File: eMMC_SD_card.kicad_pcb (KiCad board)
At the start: 4 copper layers, 100 x 74 mm, 362 parts, among them J1 SD_Card, J2 SD_Card, J3 SD_Card, J4 SD_Card, J5 SD_Card, J6 SD_Card, U1 eMMC_5.1_BGA153, U2 eMMC_5.1_BGA153, U3 eMMC_5.1_BGA153, U4 eMMC_5.1_BGA153, U5 eMMC_5.1_BGA153, U6 eMMC_5.1_BGA153

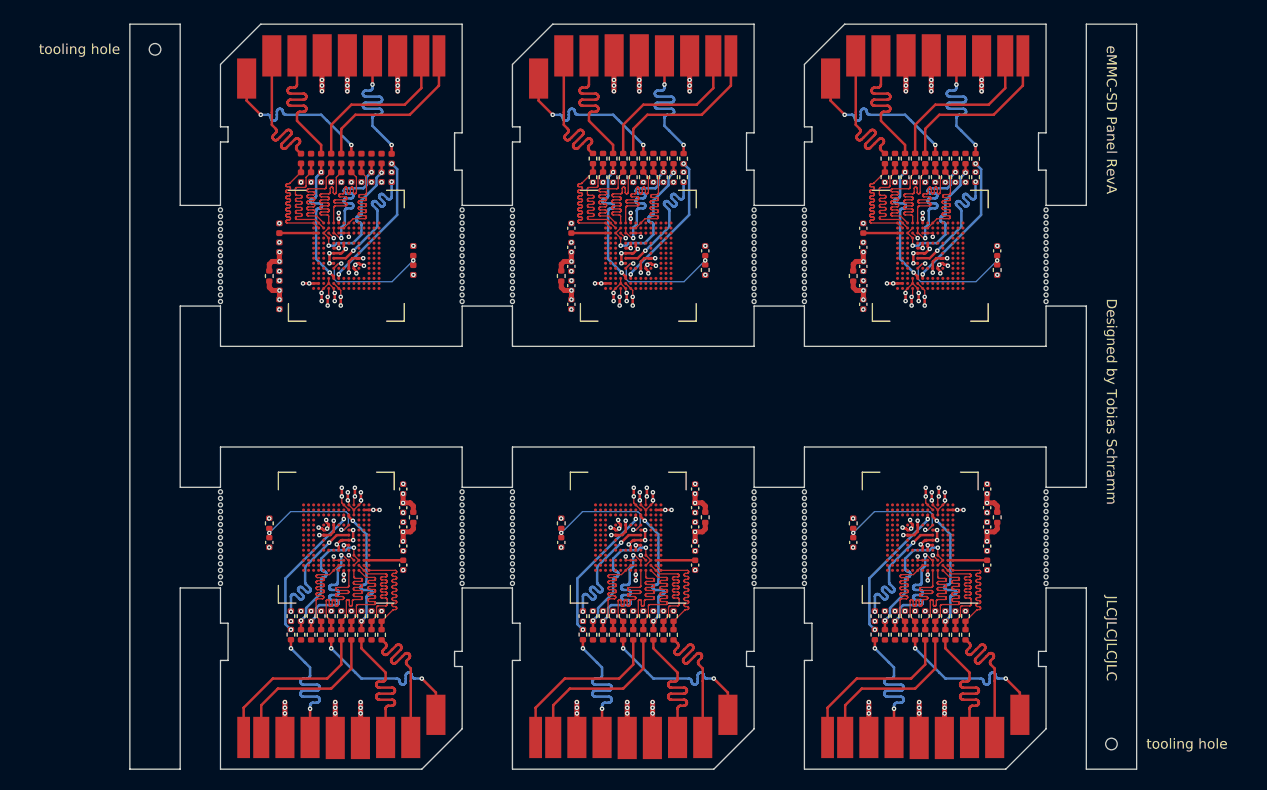
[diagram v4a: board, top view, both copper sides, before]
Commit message: Repurpose for ESP32 WiFi SDIO card
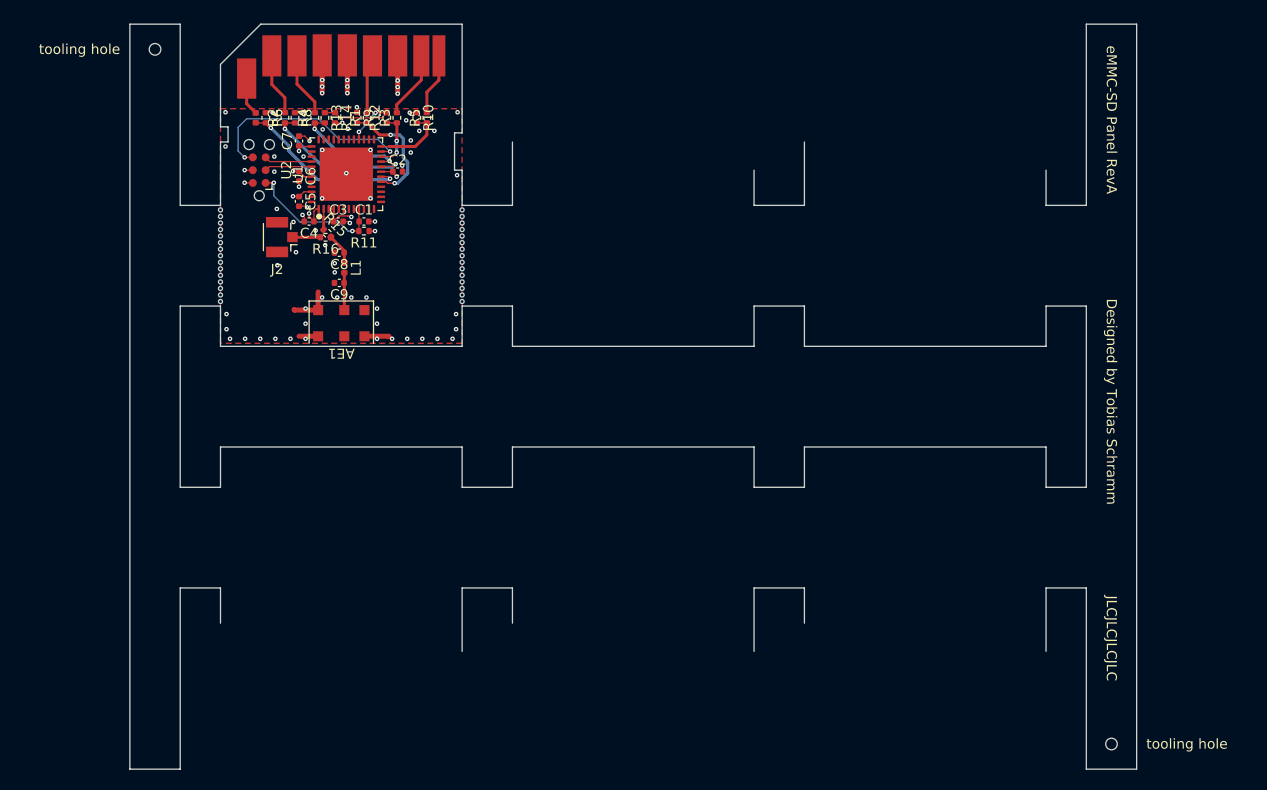
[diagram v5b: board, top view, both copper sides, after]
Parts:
- removed C10, C11, C16, C17, C22, C23, C28, C29, C34, C35: 4.7uF, Capacitor_SMD:C_0402_1005Metric
- removed C12, C13, C14, C15, C18, C19, C20, C21, C24, C25, C26, C27, C30, C31, C32, C33, C36: 100nF, Capacitor_SMD:C_0402_1005Metric
- removed H100, H101, H102, H103, H104, H105, H106, H107, H108, H109, H110, H111, H112, H113, H114, H115, H116, H117, H118, H119, H120, H121, H122, H123, H124, H125, H126, H127, H128, H129, H130, H131, H132, H133, H134, H135, H136, H137, H138, H139, H140, H141, H142, H143, H144, H145, H146, H147, H148, H149, H150, H151, H152, H153, H154, H155, H156, H157, H158, H159, H160, H161, H162, H163, H164, H165, H166, H167, H168, H169, H170, H171, H172, H173, H174, H175, H176, H177, H178, H179, H180, H31, H32, H33, H34, H35, H36, H37, H38, H39, H40, H41, H42, H43, H44, H45, H46, H47, H48, H49, H50, H51, H52, H53, H54, H55, H56, H57, H58, H59, H60, H61, H62, H63, H64, H65, H66, H67, H68, H69, H70, H71, H72, H73, H74, H75, H76, H77, H78, H79, H80, H81, H82, H83, H84, H85, H86, H87, H88, H89, H90, H91, H92, H93, H94, H95, H96, H97, H98, H99: MountingHole, Perforation:Perforation_0.4mm
- removed J3, J4, J5, J6: SD_Card, Connector_PCB_Edge_SD:SD
- removed R100, R101, R102, R103, R104, R105, R106, R107, R108, R109, R121, R122, R123, R124, R125, R126, R127, R128, R129, R130, R131, R17, R18, R19, R20, R21, R33, R34, R35, R36, R37, R38, R39, R40, R41, R42, R43, R55, R56, R57, R58, R59, R60, R61, R62, R63, R64, R65, R77, R78, R79, R80, R81, R82, R83, R84, R85, R86, R87, R99: 10kR, Resistor_SMD:R_0402_1005Metric
- removed R110, R132, R22, R44, R66, R88: 0R, Resistor_SMD:R_0402_1005Metric
- removed R111, R112, R113, R114, R115, R116, R117, R118, R119, R120, R23, R24, R25, R26, R27, R28, R29, R30, R31, R32, R45, R46, R47, R48, R49, R50, R51, R52, R53, R54, R67, R68, R69, R70, R71, R72, R73, R74, R75, R76, R89, R90, R91, R92, R93, R94, R95, R96, R97, R98: 33R, Resistor_SMD:R_0402_1005Metric
- removed U3, U4, U5, U6: eMMC_5.1_BGA153, Package_BGA_eMMC:eMMC-FBGA-153
- added AE1: Antenna_Chip, Antenna_antenova:SR4W035, F.Cu at (117.0, 129.7)
- added L1: 0R, Inductor_SMD:L_0402_1005Metric, F.Cu at (117.3, 124.2)
- C2, C3, C6: value 100nF -> 2.2uF
- C4, C5: value 4.7uF -> 2.2uF
- C8, C9: value 100nF -> DNP
- J2: value SD_Card -> Conn_Coaxial; footprint Connector_PCB_Edge_SD:SD -> Connector_Coaxial:U.FL_Hirose_U.FL-R-SMT-1_Vertical
- R10, R6, R8, R9: value 33R -> 10k
- R11, R12, R13, R14: value 10kR -> 10k
- R15, R16: value 10kR -> 0R
- U1: value eMMC_5.1_BGA153 -> ESP32-PICO-D4; footprint Package_BGA_eMMC:eMMC-FBGA-153 -> Package_DFN_QFN:QFN-48-1EP_7x7mm_P0.5mm_EP5.3x5.3mm
- U2: value eMMC_5.1_BGA153 -> TagConnect_TC2030_ESP32; footprint Package_BGA_eMMC:eMMC-FBGA-153 -> Connector:Tag-Connect_TC2030-IDC-NL_2x03_P1.27mm_Vertical
- moved C7 41.8 mm to (112.8, 111.6), turned to 90 degrees
- moved U2 38.6 mm to (108.8, 114.5), turned to 90 degrees
- moved J2 31.2 mm to (111.1, 121.2), turned to 180 degrees
- moved C9 23.3 mm to (116.8, 125.7), turned to 180 degrees
- moved C8 23.2 mm to (116.8, 122.7), turned to 180 degrees
- moved C2 13.0 mm to (122.6, 114.7), turned to 0 degrees
- moved R5 12.2 mm to (125.5, 109.3)
- moved C6 11.0 mm to (112.8, 115.1), turned to -90 degrees
- moved R2 10.4 mm to (111.4, 109.3)
- moved C5 10.4 mm to (112.8, 117.6)
- moved R6 10.3 mm to (109.5, 109.3), turned to -90 degrees
- moved R12 8.79 mm to (121.5, 109.3)
- moved R3 8.54 mm to (122.5, 109.3)
- moved R7 8.52 mm to (108.5, 109.3)
- moved U1 8.10 mm to (117.5, 114.9), turned to 90 degrees
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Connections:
- C1 pad 1: GND -> /Adapter 1/EN
- C1 pad 2: Net-(C1-Pad2) -> GND
- C2 pad 1: Net-(C2-Pad1) -> +3V3
- C3 pad 1: VCC -> +3V3
- C4 pad 1: VCC -> +3V3
- C5 pad 1: VCCQ -> +3V3
- C6 pad 1: VCCQ -> +3V3
- C7 pad 1: GND -> +3V3
- C7 pad 2: Net-(C7-Pad2) -> GND
- C9 pad 1: VCC -> Net-(AE1-Pad1)
- J1 pad 1: /Adapter 1/DAT3 -> Net-(J1-Pad1)
- J1 pad 2: /Adapter 1/CMD -> Net-(J1-Pad2)
- J1 pad 4: VCC -> +3V3
- J1 pad 5: /Adapter 1/CLK -> Net-(J1-Pad5)
- J1 pad 7: /Adapter 1/DAT0 -> Net-(J1-Pad7)
- J1 pad 8: /Adapter 1/DAT1 -> Net-(J1-Pad8)
- J1 pad 9: /Adapter 1/DAT2 -> Net-(J1-Pad9)
- J2 pad 1: /Adapter 2/DAT3 -> Net-(J2-Pad1)
- J2 pad 2: /Adapter 2/CMD -> GND
- R1 pad 1: Net-(R1-Pad1) -> /Adapter 1/CLK
- R1 pad 2: /Adapter 1/DAT2 -> Net-(J1-Pad5)
- R10 pad 1: Net-(R10-Pad1) -> +3V3
- R10 pad 2: /Adapter 1/CLK -> /Adapter 1/DAT1
- R11 pad 1: VCC -> +3V3
- R11 pad 2: Net-(C1-Pad2) -> /Adapter 1/EN
- R12 pad 1: VCC -> /Adapter 1/DAT0
- R13 pad 1: VCC -> Net-(R12-Pad2)
- R13 pad 2: /Adapter 1/D7 -> /Adapter 1/CMD
- R14 pad 1: VCC -> Net-(R12-Pad2)
- R14 pad 2: /Adapter 1/D6 -> GND
- R15 pad 1: VCC -> Net-(U1-Pad2)
- R15 pad 2: /Adapter 1/D5 -> Net-(C8-Pad1)
- R16 pad 1: VCC -> Net-(C8-Pad1)
- R16 pad 2: /Adapter 1/D4 -> Net-(J2-Pad1)
- R2 pad 1: /Adapter 1/D5 -> /Adapter 1/DAT3
- R2 pad 2: Net-(R2-Pad2) -> Net-(J1-Pad1)
- R3 pad 1: Net-(R12-Pad2) -> /Adapter 1/DAT0
- R3 pad 2: /Adapter 1/CMD -> Net-(J1-Pad7)
- R4 pad 1: Net-(R19-Pad2) -> /Adapter 1/CMD
- R4 pad 2: /Adapter 1/DAT1 -> Net-(J1-Pad2)
- R5 pad 1: /Adapter 1/D4 -> /Adapter 1/DAT1
- R5 pad 2: Net-(R5-Pad2) -> Net-(J1-Pad8)
- R6 pad 1: /Adapter 1/D7 -> +3V3
- R6 pad 2: Net-(R6-Pad2) -> /Adapter 1/DAT2
- R7 pad 1: Net-(R20-Pad2) -> /Adapter 1/DAT2
- R7 pad 2: /Adapter 1/DAT0 -> Net-(J1-Pad9)
- R8 pad 1: /Adapter 1/D3 -> +3V3
- R9 pad 1: /Adapter 1/D6 -> +3V3
- R9 pad 2: Net-(R9-Pad2) -> /Adapter 1/CLK
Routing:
- net GND: track 128.9 -> 23.0 mm, vias 162 -> 66
- net (no net): track 56.4 -> 0.00 mm
- net VCC: track 55.8 -> 0.00 mm, vias 114 -> 0
- net VCCQ: track 52.0 -> 0.00 mm, vias 42 -> 0
- net +3V3: track 0.00 -> 22.0 mm, vias 0 -> 15
- net /Adapter 1/IO0: track 0.00 -> 21.8 mm, vias 0 -> 2
- net /Adapter 3/DAT2: track 16.9 -> 0.00 mm, vias 2 -> 0
- net /Adapter 2/DAT2: track 16.9 -> 0.00 mm, vias 2 -> 0
- net /Adapter 6/DAT2: track 16.9 -> 0.00 mm, vias 2 -> 0
- net /Adapter 5/DAT2: track 16.9 -> 0.00 mm, vias 2 -> 0
- net /Adapter 4/DAT2: track 16.9 -> 0.00 mm, vias 2 -> 0
- net /Adapter 3/CMD: track 16.9 -> 0.00 mm
- net /Adapter 2/CMD: track 16.9 -> 0.00 mm
- net /Adapter 6/CMD: track 16.9 -> 0.00 mm
- net /Adapter 5/CMD: track 16.9 -> 0.00 mm
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- added copper zone on In2.Cu, net +3V3
- added copper zone on F.Cu, net GND
- added copper zone on In1.Cu, net GND
- removed copper zone on GND, net GND
- removed copper zone on VCC, net VCC
- removed copper zone on VCC, net VCCQ
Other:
- net class Default removed

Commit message: Add project icon to PCB
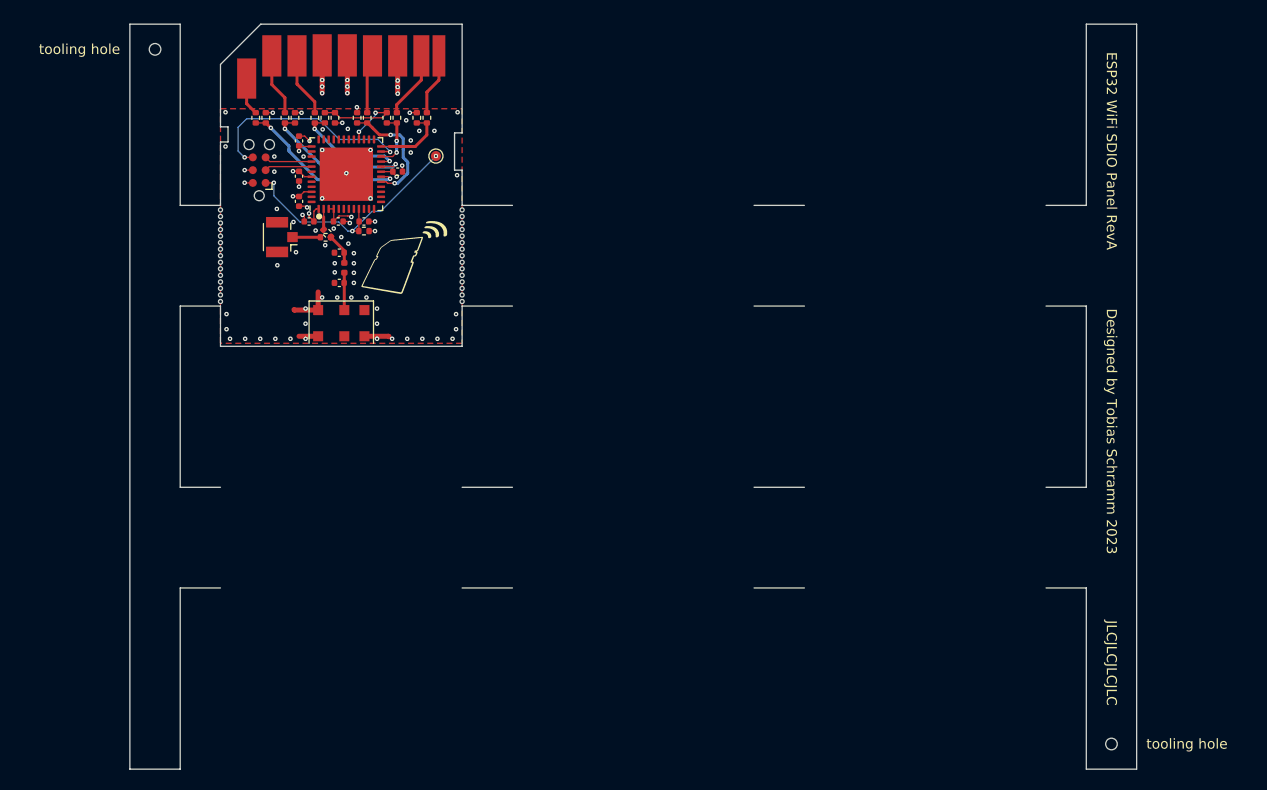
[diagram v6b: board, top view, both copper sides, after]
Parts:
- added G***: LOGO, Icons:wlan_sd, F.Cu at (123.2, 123.2)
- added TP1: RESET, TestPoint:TestPoint_Pad_D1.0mm, F.Cu at (126.4, 113.1)
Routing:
- net /Adapter 1/EN: track 14.3 -> 25.7 mm, vias 2 -> 3
- net /Adapter 1/IO0: track 21.8 -> 22.3 mm
- net GND: vias 66 -> 73
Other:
- outline, holes or cut-outs redrawn
- board text added: "Designed by Tobias Schramm 2023"
- board text added: "ESP32 WLAN SDIO card RevA"
- board text added: "ESP32 WiFi SDIO Panel RevA"
- board text added: "Tobias Schramm 2023"
- board text removed: "8GB"
- board text removed: "Designed by Tobias Schramm"
- board text removed: "by Tobias Schramm"
- board text removed: "eMMC-SD"
- board text removed: "eMMC-SD Panel RevA"
